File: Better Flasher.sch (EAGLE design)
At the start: 7 parts, among them IC2 NE555, J1 1X2-3.5MM

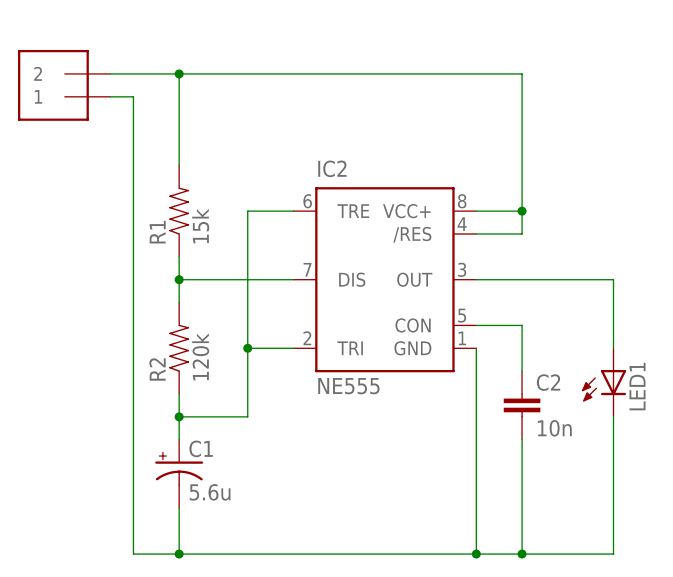
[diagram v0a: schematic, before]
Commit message: Additional modifications to repaired design
Changes were made based on comments
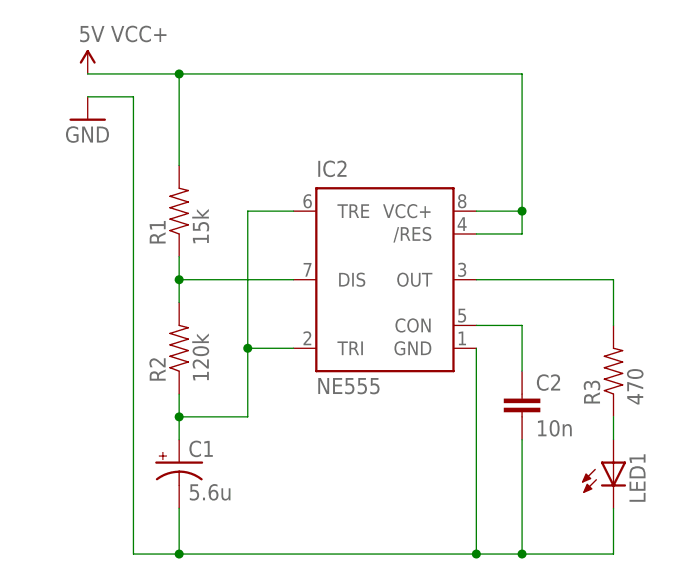
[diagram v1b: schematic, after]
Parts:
- removed J1: 1X2-3.5MM, adafruit:1X2-3.5MM
- added R3: 470, SparkFun-Resistors:RESISTORAXIAL-0.3
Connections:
- removed net N$6: IC2.OUT, LED1.A
- new net N$1: IC2.OUT, R3.2
- new net N$5: LED1.A, R3.1
- net GND: no longer J1.1
- net VCC+: no longer J1.2
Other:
- moved on the sheet: LED1
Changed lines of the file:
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@@
 <part name="LED1" library="adafruit" deviceset="LED" device="5MM"/>
 <part name="C2" library="SparkFun-Capacitors" deviceset="CAP" device="PTH" value="10n"/>
-<part name="J1" library="adafruit" deviceset="1X2" device="-3.5MM"/>
+<part name="R3" library="SparkFun-Resistors" deviceset="RESISTOR" device="AXIAL-0.3" value="470"/>
+<part name="SUPPLY1" library="SparkFun-Aesthetics" deviceset="VCC" device="" value="5V VCC+"/>
+<part name="GND1" library="SparkFun-Aesthetics" deviceset="GND" device=""/>
 </parts>
 <sheets>
@@
 <instance part="R2" gate="G$1" x="10.16" y="68.58" rot="R90"/>
 <instance part="C1" gate="G$1" x="10.16" y="55.88"/>
-<instance part="LED1" gate="G$1" x="58.42" y="66.04"/>
+<instance part="LED1" gate="G$1" x="58.42" y="55.88"/>
 <instance part="C2" gate="G$1" x="48.26" y="60.96"/>
-<instance part="J1" gate="G$1" x="-2.54" y="99.06" rot="R180"/>
+<instance part="R3" gate="G$1" x="58.42" y="66.04" rot="R90"/>
+<instance part="SUPPLY1" gate="G$1" x="0" y="99.06"/>
+<instance part="GND1" gate="1" x="0" y="93.98"/>
 </instances>
 <busses>
 </busses>
 <nets>
-<net name="VCC+" class="0">
-<segment>
-<pinref part="J1" gate="G$1" pin="2"/>
-<wire x1="2.54" y1="99.06" x2="10.16" y2="99.06" width="0.1524" layer="91"/>
-<wire x1="10.16" y1="99.06" x2="48.26" y2="99.06" width="0.1524" layer="91"/>
-<wire x1="48.26" y1="99.06" x2="48.26" y2="83.82" width="0.1524" layer="91"/>
-<pinref part="IC2" gate="G$1" pin="VCC+"/>
-<wire x1="48.26" y1="83.82" x2="43.18" y2="83.82" width="0.1524" layer="91"/>
-<pinref part="IC2" gate="G$1" pin="/RES"/>
-<wire x1="43.18" y1="81.28" x2="48.26" y2="81.28" width="0.1524" layer="91"/>
-<wire x1="48.26" y1="81.28" x2="48.26" y2="83.82" width="0.1524" layer="91"/>
-<junction x="48.26" y="83.82"/>
-<pinref part="R1" gate="G$1" pin="2"/>
-<wire x1="10.16" y1="88.9" x2="10.16" y2="99.06" width="0.1524" layer="91"/>
-<junction x="10.16" y="99.06"/>
-</segment>
-</net>
 <net name="N$2" class="0">
 <segment>
@@
 <net name="GND" class="0">
 <segment>
-<pinref part="J1" gate="G$1" pin="1"/>
-<wire x1="2.54" y1="96.52" x2="5.08" y2="96.52" width="0.1524" layer="91"/>
 <wire x1="5.08" y1="96.52" x2="5.08" y2="45.72" width="0.1524" layer="91"/>
 <pinref part="C2" gate="G$1" pin="2"/>
@@
 <junction x="10.16" y="45.72"/>
 <pinref part="LED1" gate="G$1" pin="C"/>
-<wire x1="58.42" y1="60.96" x2="58.42" y2="45.72" width="0.1524" layer="91"/>
+<wire x1="58.42" y1="50.8" x2="58.42" y2="45.72" width="0.1524" layer="91"/>
 <wire x1="58.42" y1="45.72" x2="48.26" y2="45.72" width="0.1524" layer="91"/>
 <junction x="48.26" y="45.72"/>
+<pinref part="GND1" gate="1" pin="GND"/>
+<wire x1="5.08" y1="96.52" x2="0" y2="96.52" width="0.1524" layer="91"/>
 </segment>
 </net>
-<net name="N$6" class="0">
+<net name="N$1" class="0">
 <segment>
 <pinref part="IC2" gate="G$1" pin="OUT"/>
-<pinref part="LED1" gate="G$1" pin="A"/>
+<pinref part="R3" gate="G$1" pin="2"/>
 <wire x1="43.18" y1="76.2" x2="58.42" y2="76.2" width="0.1524" layer="91"/>
-<wire x1="58.42" y1="76.2" x2="58.42" y2="68.58" width="0.1524" layer="91"/>
+<wire x1="58.42" y1="76.2" x2="58.42" y2="71.12" width="0.1524" layer="91"/>
 </segment>
 </net>
+<net name="N$5" class="0">
+<segment>
+<pinref part="R3" gate="G$1" pin="1"/>
+<pinref part="LED1" gate="G$1" pin="A"/>
+<wire x1="58.42" y1="60.96" x2="58.42" y2="58.42" width="0.1524" layer="91"/>
+</segment>
+</net>
+<net name="VCC+" class="0">
+<segment>
+<wire x1="10.16" y1="99.06" x2="48.26" y2="99.06" width="0.1524" layer="91"/>
+<wire x1="48.26" y1="99.06" x2="48.26" y2="83.82" width="0.1524" layer="91"/>
+<pinref part="IC2" gate="G$1" pin="VCC+"/>
+<wire x1="48.26" y1="83.82" x2="43.18" y2="83.82" width="0.1524" layer="91"/>
+<pinref part="IC2" gate="G$1" pin="/RES"/>
+<wire x1="43.18" y1="81.28" x2="48.26" y2="81.28" width="0.1524" layer="91"/>
+<wire x1="48.26" y1="81.28" x2="48.26" y2="83.82" width="0.1524" layer="91"/>
+<junction x="48.26" y="83.82"/>
+<pinref part="R1" gate="G$1" pin="2"/>
+<wire x1="10.16" y1="88.9" x2="10.16" y2="99.06" width="0.1524" layer="91"/>
+<pinref part="SUPPLY1" gate="G$1" pin="VCC"/>
+<wire x1="0" y1="99.06" x2="10.16" y2="99.06" width="0.1524" layer="91"/>
+<junction x="10.16" y="99.06"/>
+</segment>
+</net>
